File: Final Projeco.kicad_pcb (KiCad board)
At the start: 6 copper layers, 26.5 x 45 mm, 29 parts, among them U1 ESP32-S3, U2 GT-USB-7004N, U3 NCP167BMX330TBG, U4 LY68L6400SLIT, U5 PTS830GG140SMTRLFS, U6 PTS830GG140SMTRLFS, U7 220S-2*16P_H=8_5MM_Ytype_L=3_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, X1 TZ1269D

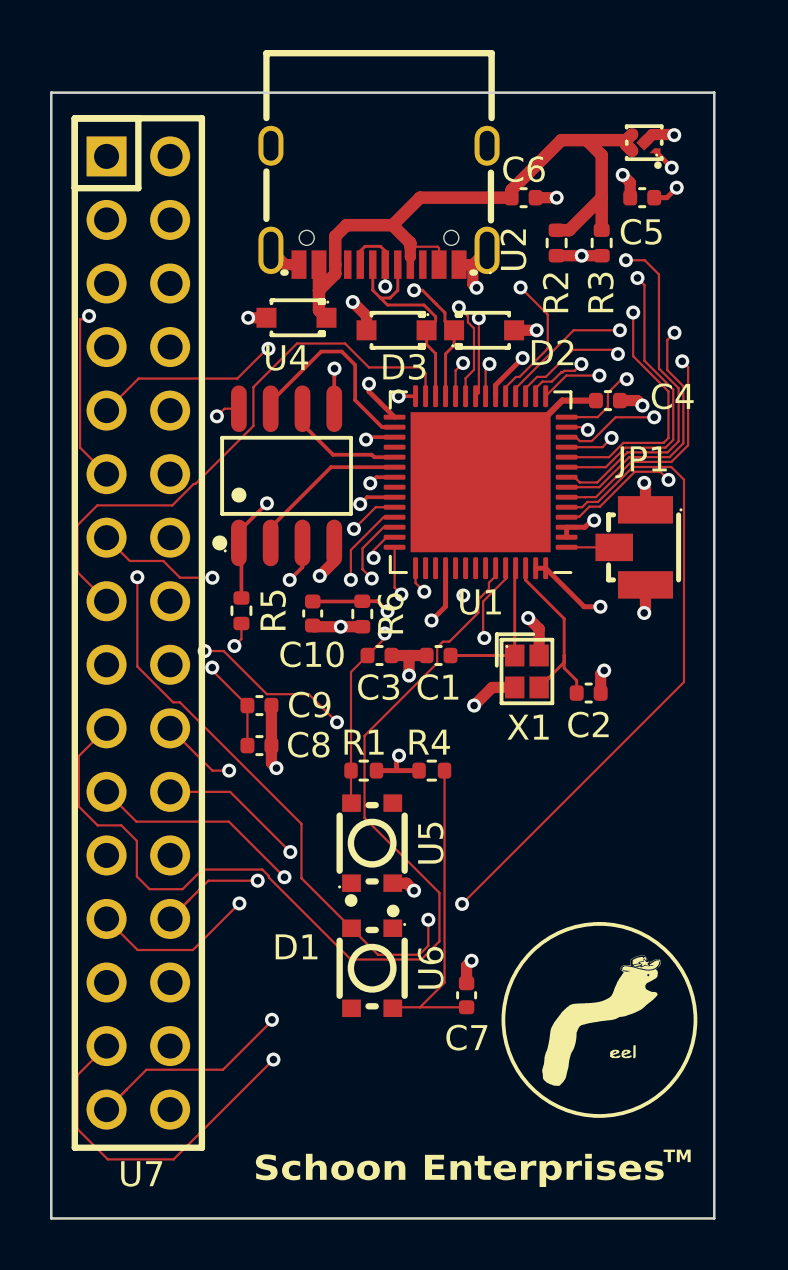
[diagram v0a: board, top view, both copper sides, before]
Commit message: -Final Draft Submission mk2
-Added bypass caps across 3.3 & GND to make signal less ripple-y
-added component to replace SRAM chip:
https://jlcpcb.com/partdetail/Zetta-ZD25Q32CTIGT/C3029778
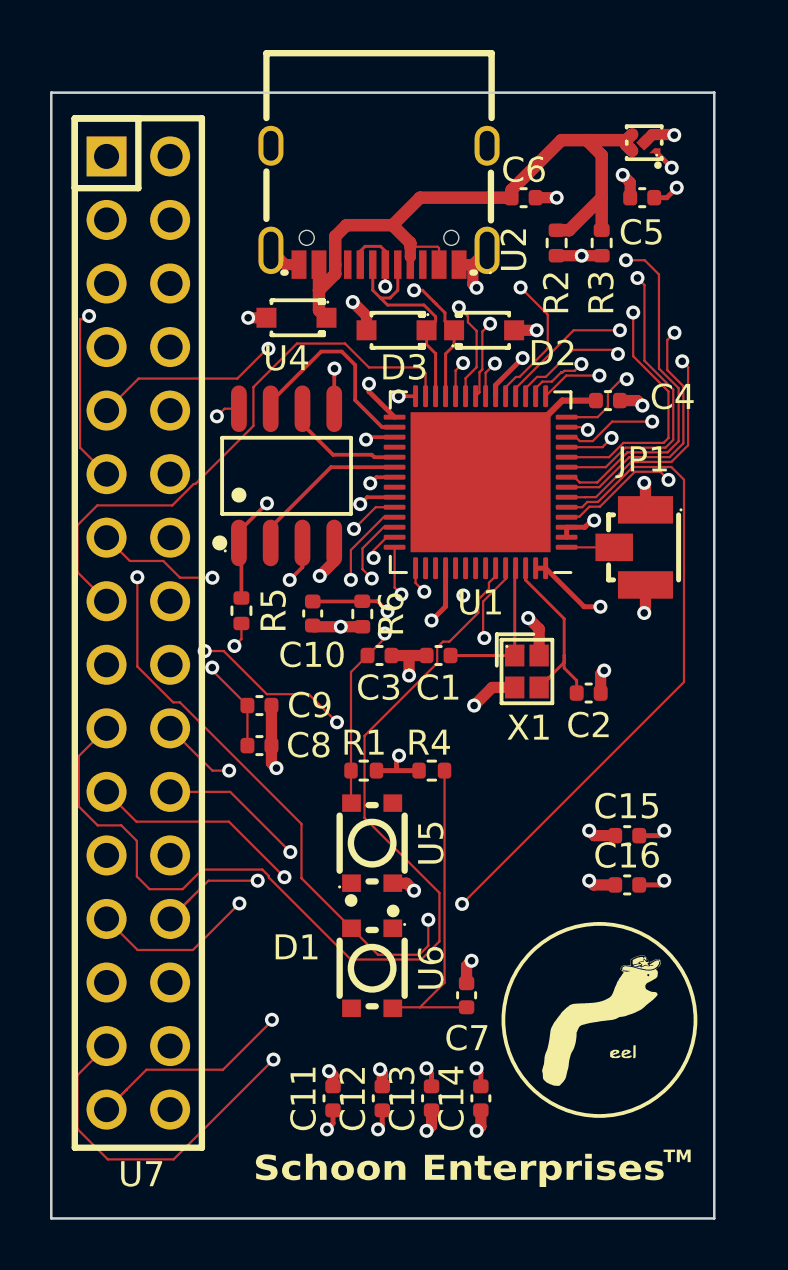
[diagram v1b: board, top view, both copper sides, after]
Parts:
- added C11: 1uF, Capacitor_SMD:C_0402_1005Metric, F.Cu at (36.3, 55.7)
- added C12: 1uF, Capacitor_SMD:C_0402_1005Metric, F.Cu at (38.2, 55.7)
- added C13: 0.1uF, Capacitor_SMD:C_0402_1005Metric, F.Cu at (40.2, 55.7)
- added C14: 0.1uF, Capacitor_SMD:C_0402_1005Metric, F.Cu at (42.2, 55.7)
- added C15: 0.1uF, Capacitor_SMD:C_0402_1005Metric, F.Cu at (48.0, 45.2)
- added C16: 0.1uF, Capacitor_SMD:C_0402_1005Metric, F.Cu at (48.0, 47.2)
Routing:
- net VDD3P3: track 15.2 -> 20.7 mm, vias 8 -> 14
- net GND: track 30.8 -> 36.2 mm, vias 20 -> 26
- net /GPIO16: track 19.6 -> 20.3 mm
